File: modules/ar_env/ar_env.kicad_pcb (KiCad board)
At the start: 2 copper layers, 30.5 x 68.6 mm, 4 parts

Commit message: Finalize the PCB
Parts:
- added C1: 0.1uf, Capacitor_SMD:C_0402_1005Metric, F.Cu at (68.2, 55.7)
- added C2: 1uf, Capacitor_SMD:C_1206_3216Metric, F.Cu at (71.7, 96.6)
- added C3: 0.1uf, Capacitor_SMD:C_0402_1005Metric, F.Cu at (53.5, 74.0)
- added D1: 1N4148WS, Diode_SMD:D_SOD-323_HandSoldering, F.Cu at (57.1, 56.2)
- added D2: 1N4148WS, Diode_SMD:D_SOD-323_HandSoldering, F.Cu at (72.5, 67.7)
- added D3: 1N4148WS, Diode_SMD:D_SOD-323_HandSoldering, F.Cu at (72.5, 72.4)
- added D4: LED, LED_SMD:LED_0603_1608Metric, F.Cu at (72.6, 63.1)
- added R3: 100k, Resistor_SMD:R_0402_1005Metric, F.Cu at (55.9, 59.2)
- added R4: 100k, Resistor_SMD:R_0402_1005Metric, F.Cu at (58.9, 58.7)
- added R5: 6.8k, Resistor_SMD:R_0402_1005Metric, F.Cu at (55.9, 54.5)
- added R6: 1k, Resistor_SMD:R_0402_1005Metric, F.Cu at (50.3, 74.0)
- added R7: 1k, Resistor_SMD:R_0402_1005Metric, F.Cu at (53.3, 63.1)
- added RV1: 5k, BreadModular_Pots:Potentiometer_RV09, F.Cu at (59.7, 73.0)
- added RV2: 1M, BreadModular_Pots:Potentiometer_RV09, F.Cu at (52.1, 89.5)
- added RV3: 1M, BreadModular_Pots:Potentiometer_RV09, F.Cu at (67.3, 89.5)
- added U1: MCP6002-xSN, Package_SO:SOIC-8-1EP_3.9x4.9mm_P1.27mm_EP2.29x3mm, F.Cu at (63.5, 57.4)
- added U2: MCP6002-xSN, Package_SO:SOIC-8-1EP_3.9x4.9mm_P1.27mm_EP2.29x3mm, F.Cu at (51.7, 68.1)
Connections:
- INPUT1 pad 1: unconnected-(INPUT1-Pin_1-Pad1) -> V_IN
- INPUT1 pad 2: unconnected-(INPUT1-Pin_2-Pad2) -> Net-(INPUT1-Pin_2)
- INPUT1 pad 3: unconnected-(INPUT1-Pin_3-Pad3) -> Net-(INPUT1-Pin_2)
- INPUT1 pad 4: unconnected-(INPUT1-Pin_4-Pad4) -> Net-(INPUT1-Pin_2)
- INPUT1 pad 5: unconnected-(INPUT1-Pin_5-Pad5) -> Net-(INPUT1-Pin_2)
- OUTPUT2 pad 1: unconnected-(OUTPUT2-Pin_1-Pad1) -> V_OUT
- OUTPUT2 pad 2: unconnected-(OUTPUT2-Pin_2-Pad2) -> V_OUT
- OUTPUT2 pad 3: unconnected-(OUTPUT2-Pin_3-Pad3) -> V_OUT
- OUTPUT2 pad 4: unconnected-(OUTPUT2-Pin_4-Pad4) -> V_OUT
- OUTPUT2 pad 5: unconnected-(OUTPUT2-Pin_5-Pad5) -> V_OUT
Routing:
- net GND: track 10.2 -> 207.1 mm, vias 0 -> 4
- net V_SHAPE: track 0.00 -> 70.3 mm
- net V_OUT: track 0.00 -> 57.4 mm, vias 0 -> 2
- net +5V: track 10.2 -> 58.1 mm, vias 0 -> 4
- net Net-(D2-K): track 0.00 -> 44.2 mm, vias 0 -> 2
- net Net-(D2-A): track 0.00 -> 33.3 mm
- net Net-(U1A--): track 0.00 -> 24.1 mm, vias 0 -> 2
- net Net-(D4-A): track 0.00 -> 20.8 mm
- net Net-(D3-A): track 0.00 -> 19.8 mm, vias 0 -> 2
- net V_IN: track 0.00 -> 16.5 mm
- net Net-(INPUT1-Pin_2): track 0.00 -> 7.62 mm
- net Net-(U2A--): track 0.00 -> 4.70 mm
- net Net-(D1-K): track 0.00 -> 4.34 mm
- net Net-(U2B--): track 0.00 -> 4.03 mm
- net Net-(D1-A): track 0.00 -> 3.18 mm
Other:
- board text added: "ATTACK"
- board text added: "ENV"
- board text added: "INPUT"
- board text added: "MULT"
- board text added: "OUTPUT"
- board text added: "RELEASE"
- board text added: "SHAPE"
- board text added: "SIG"

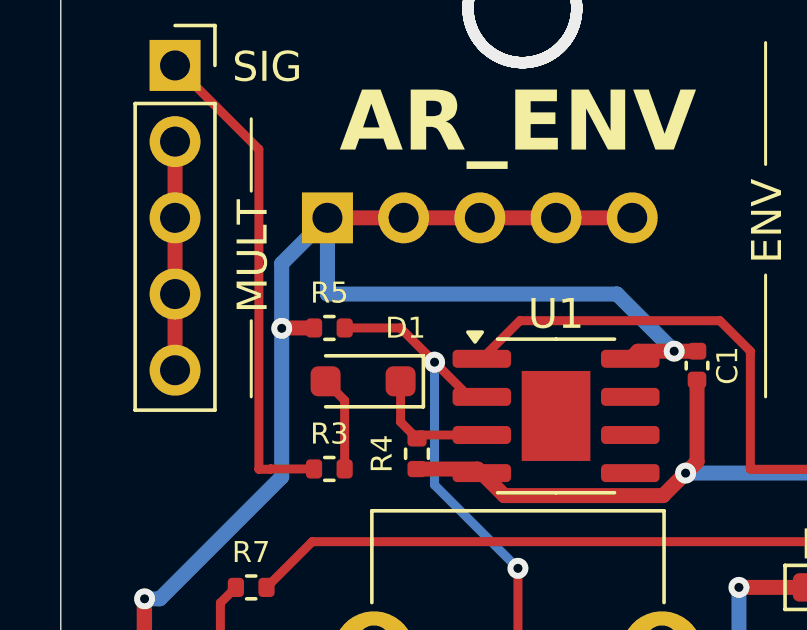
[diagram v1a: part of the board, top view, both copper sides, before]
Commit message: Changed the 6.8k resistor package. Used 0603 package due to availability in JLCPCB
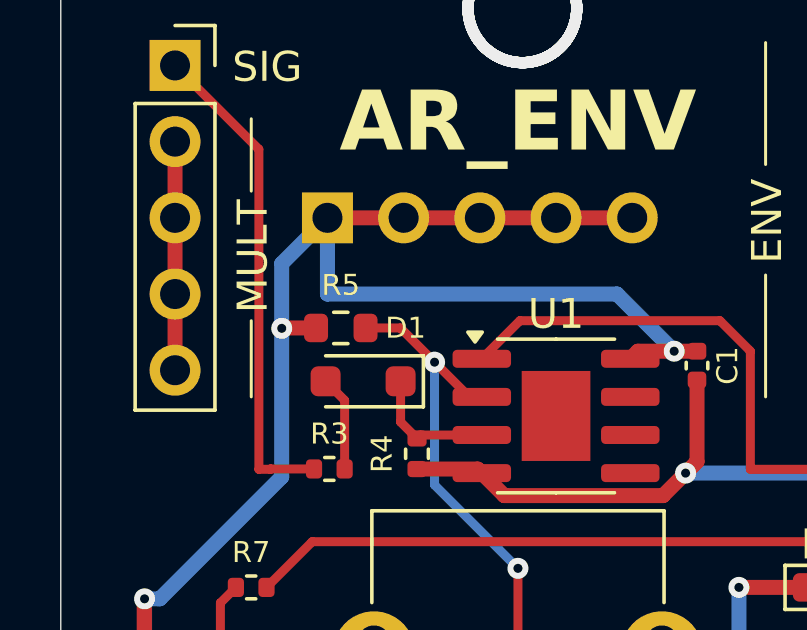
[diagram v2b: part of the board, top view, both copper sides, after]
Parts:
- R5: footprint Resistor_SMD:R_0402_1005Metric -> Resistor_SMD:R_0603_1608Metric
- moved R5 0.38 mm to (56.3, 54.5)
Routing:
- net Net-(U1A--): track 24.1 -> 23.4 mm
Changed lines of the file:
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@@
 		)
 	)
-	(footprint "Resistor_SMD:R_0402_1005Metric"
+	(footprint "Resistor_SMD:R_0603_1608Metric"
 		(layer "F.Cu")
-		(at 55.945 54.471)
-		(descr "Resistor SMD 0402 (1005 Metric), square (rectangular) end terminal, IPC_7351 nominal, (Body size source: IPC-SM-782 page 72, https://www.pcb-3d.com/wordpress/wp-content/uploads/ipc-sm-782a_amendment_1_and_2.pdf), generated with kicad-footprint-generator")
+		(at 56.325 54.471)
+		(descr "Resistor SMD 0603 (1608 Metric), square (rectangular) end terminal, IPC_7351 nominal, (Body size source: IPC-SM-782 page 72, https://www.pcb-3d.com/wordpress/wp-content/uploads/ipc-sm-782a_amendment_1_and_2.pdf), generated with kicad-footprint-generator")
 		(tags "resistor")
 		(property "Reference" "R5"
-			(at 0 -1.17 0)
+			(at 0 -1.43 0)
 			(layer "F.SilkS")
 			(effects
@@
 		)
 		(property "Value" "6.8k"
-			(at 0 1.17 0)
+			(at 0 1.43 0)
 			(layer "F.Fab")
 			(effects
 				(font
-					(size 0.5 0.5)
-					(thickness 0.1)
-					(bold yes)
+					(size 1 1)
+					(thickness 0.15)
 				)
 			)
 		)
-		(property "Footprint" "Resistor_SMD:R_0402_1005Metric"
+		(property "Footprint" "Resistor_SMD:R_0603_1608Metric"
 			(at 0 0 0)
 			(unlocked yes)
@@
 		(attr smd)
 		(fp_line
-			(start -0.153641 -0.38)
-			(end 0.153641 -0.38)
+			(start -0.237258 -0.5225)
+			(end 0.237258 -0.5225)
 			(stroke
 				(width 0.12)
@@
 		)
 		(fp_line
-			(start -0.153641 0.38)
-			(end 0.153641 0.38)
+			(start -0.237258 0.5225)
+			(end 0.237258 0.5225)
 			(stroke
 				(width 0.12)
@@
 		)
 		(fp_line
-			(start -0.93 -0.47)
-			(end 0.93 -0.47)
+			(start -1.48 -0.73)
+			(end 1.48 -0.73)
 			(stroke
 				(width 0.05)
@@
 		)
 		(fp_line
-			(start -0.93 0.47)
-			(end -0.93 -0.47)
+			(start -1.48 0.73)
+			(end -1.48 -0.73)
 			(stroke
 				(width 0.05)
@@
 		)
 		(fp_line
-			(start 0.93 -0.47)
-			(end 0.93 0.47)
+			(start 1.48 -0.73)
+			(end 1.48 0.73)
 			(stroke
 				(width 0.05)
@@
 		)
 		(fp_line
-			(start 0.93 0.47)
-			(end -0.93 0.47)
+			(start 1.48 0.73)
+			(end -1.48 0.73)
 			(stroke
 				(width 0.05)
@@
 		)
 		(fp_line
-			(start -0.525 -0.27)
-			(end 0.525 -0.27)
+			(start -0.8 -0.4125)
+			(end 0.8 -0.4125)
 			(stroke
 				(width 0.1)
@@
 		)
 		(fp_line
-			(start -0.525 0.27)
-			(end -0.525 -0.27)
+			(start -0.8 0.4125)
+			(end -0.8 -0.4125)
 			(stroke
 				(width 0.1)
@@
 		)
 		(fp_line
-			(start 0.525 -0.27)
-			(end 0.525 0.27)
+			(start 0.8 -0.4125)
+			(end 0.8 0.4125)
 			(stroke
 				(width 0.1)
@@
 		)
 		(fp_line
-			(start 0.525 0.27)
-			(end -0.525 0.27)
+			(start 0.8 0.4125)
+			(end -0.8 0.4125)
 			(stroke
 				(width 0.1)
@@
 			(effects
 				(font
-					(size 0.26 0.26)
-					(thickness 0.04)
+					(size 0.4 0.4)
+					(thickness 0.06)
 				)
 			)
 		)
 		(pad "1" smd roundrect
-			(at -0.51 0)
-			(size 0.54 0.64)
+			(at -0.825 0)
+			(size 0.8 0.95)
 			(layers "F.Cu" "F.Paste" "F.Mask")
 			(roundrect_rratio 0.25)
@@
 		)
 		(pad "2" smd roundrect
-			(at 0.51 0)
-			(size 0.54 0.64)
+			(at 0.825 0)
+			(size 0.8 0.95)
 			(layers "F.Cu" "F.Paste" "F.Mask")
 			(roundrect_rratio 0.25)
@@
 			(pintype "passive")
 		)
-		(model "${KICAD8_3DMODEL_DIR}/Resistor_SMD.3dshapes/R_0402_1005Metric.wrl"
+		(model "${KICAD8_3DMODEL_DIR}/Resistor_SMD.3dshapes/R_0603_1608Metric.wrl"
 			(offset
 				(xyz 0 0 0)
@@
 	)
 	(segment
-		(start 55.435 54.471)
-		(end 54.368 54.471)
-		(width 0.5)
-		(layer "F.Cu")
-		(net 2)
-	)
-	(segment
 		(start 49.772 63.512)
 		(end 49.784 63.5)
@@
 	)
 	(segment
+		(start 55.5 54.471)
+		(end 54.368 54.471)
+		(width 0.5)
+		(layer "F.Cu")
+		(net 2)
+	)
+	(segment
 		(start 55.88 50.8)
 		(end 66.04 50.8)
@@
 	(segment
 		(start 58.310738 54.471)
-		(end 56.455 54.471)
+		(end 59.450869 55.611131)
 		(width 0.3)
 		(layer "F.Cu")
@@
 	)
 	(segment
-		(start 59.450869 55.611131)
+		(start 57.15 54.471)
 		(end 58.310738 54.471)
 		(width 0.3)
